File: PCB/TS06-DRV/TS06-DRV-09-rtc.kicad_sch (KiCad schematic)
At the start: 1 part, among them U13 DS3231 mini

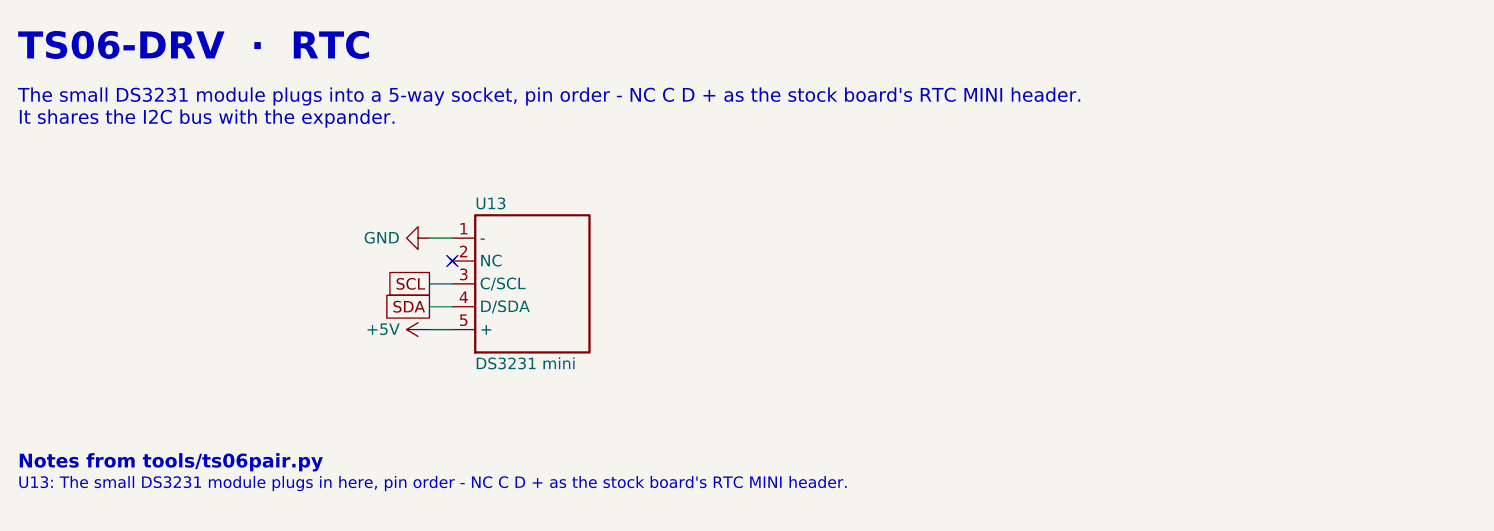
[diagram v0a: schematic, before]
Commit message: TS06-DRV rev B: routed - round 13, 0 nets sharing, 0 unrouted; board, rules and schematic written
The route of run r3 (PYTHONHASHSEED=0, the RC block of OPTIONS.md option 3),
polished (30 nets shorter), saved in tools/mkpcb_drv_routes.json, and the board
regenerated from it: check() 0 problems, 0 cathode pads under 0.5 mm, check_mate()
clean, 1164 segments, 0 vias. TS06-DRV.kicad_dru carries the 0.8 mm HV pad rule.
Schematic regenerated by tools/mksch_pair.py; BOMs unchanged by tools/bom_pair.py.

State: board written from a converged route; verify_pair not yet run.
Blocker: none.
Next: verify_pair.sh, scorecard, README row.

Co-Authored-By: Claude Opus 5.5 <noreply@anthropic.com>
Claude-Session: https://claude.ai/code/session_01WoV3gyAFgmtuk6W6Dr4bdA
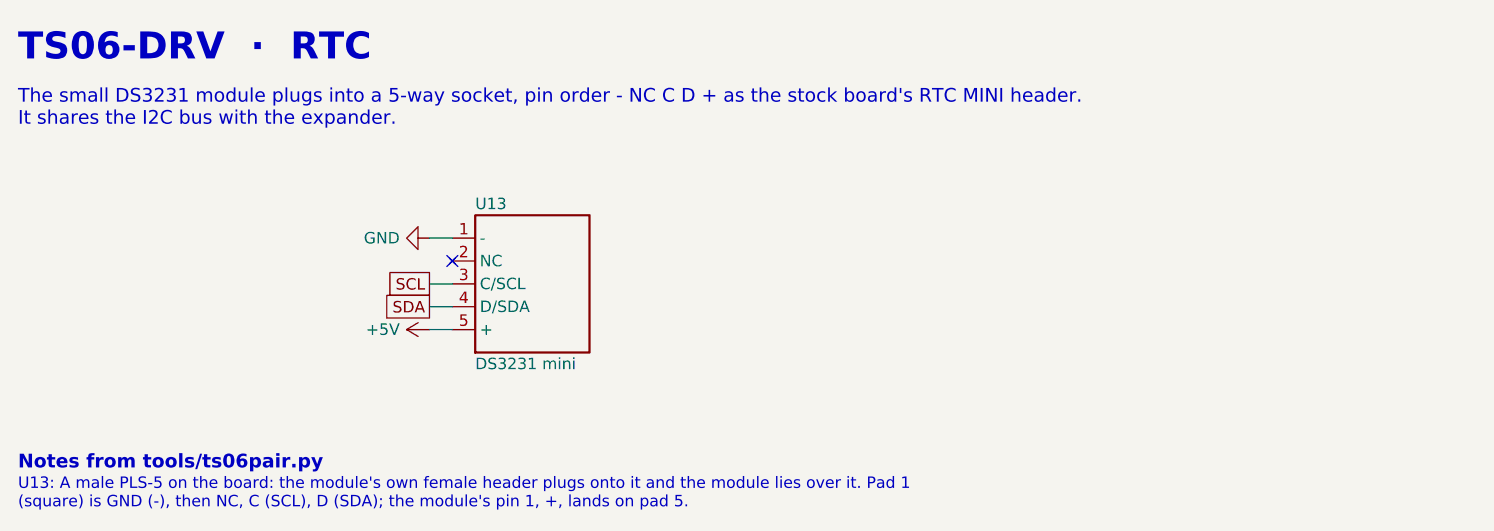
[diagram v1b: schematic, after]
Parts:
- U13: footprint TS06:TS06_PinSocket_1x05_R270 -> TS06:TS06_PinHeader_1x05_DS3231_R270
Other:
- note added: "U13: A male PLS-5 on the board: the module's own female header plugs onto it and the module lies over it. Pad 1 (square) is GND (-), then NC, C (SCL), D (SDA); the module's pin 1, +, lands on pad 5."
- note removed: "U13: The small DS3231 module plugs in here, pin order - NC C D + as the stock board's RTC MINI header."
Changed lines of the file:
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@@
 )
 )
-(text "U13: The small DS3231 module plugs in here, pin order - NC C D + as the stock board's RTC MINI header."
+(text "U13: A male PLS-5 on the board: the module's own female header plugs onto it and the module lies over it. Pad 1\n(square) is GND (-), then NC, C (SCL), D (SDA); the module's pin 1, +, lands on pad 5."
 (exclude_from_sim no)
 (at 20.32 62.23 0)
@@
 )
 )
-(property "Footprint" "TS06:TS06_PinSocket_1x05_R270"
+(property "Footprint" "TS06:TS06_PinHeader_1x05_DS3231_R270"
 (at 76.2 40.64 0)
 (hide yes)
@@
 (on_board yes)
 (dnp no)
-(property "Reference" "#PWR073"
+(property "Reference" "#PWR078"
 (at 66.04 45.72 0)
 (hide yes)
@@
 (project "TS06-DRV"
 (path "/581aa1b9-f775-5fe0-87f7-a79eaeda6019/9a8a918d-3cba-515a-8185-9a53d711dcc0"
-(reference "#PWR073")
+(reference "#PWR078")
 (unit 1)
 )
@@
 (on_board yes)
 (dnp no)
-(property "Reference" "#PWR074"
+(property "Reference" "#PWR079"
 (at 66.04 35.56 0)
 (hide yes)
@@
 (project "TS06-DRV"
 (path "/581aa1b9-f775-5fe0-87f7-a79eaeda6019/9a8a918d-3cba-515a-8185-9a53d711dcc0"
-(reference "#PWR074")
-(unit 1)
-)
+(reference "#PWR079")
+(unit 1)
+)
